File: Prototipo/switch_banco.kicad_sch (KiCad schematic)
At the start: 9 parts

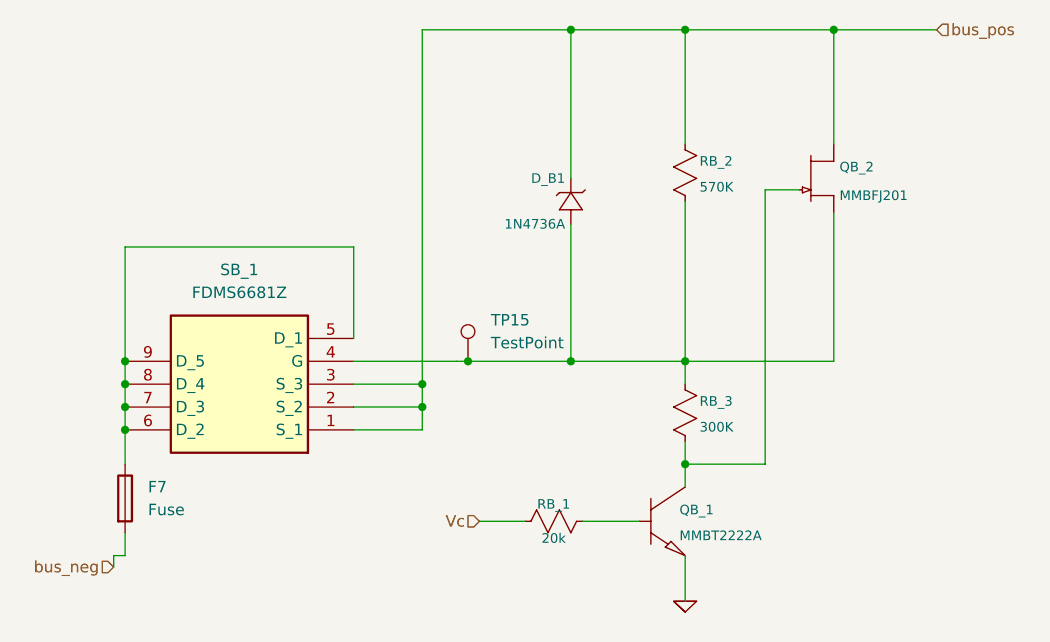
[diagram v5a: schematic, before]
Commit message: termino de reacomodar las celdas con la disposición nueva, faltan las conexiones de la entrada.
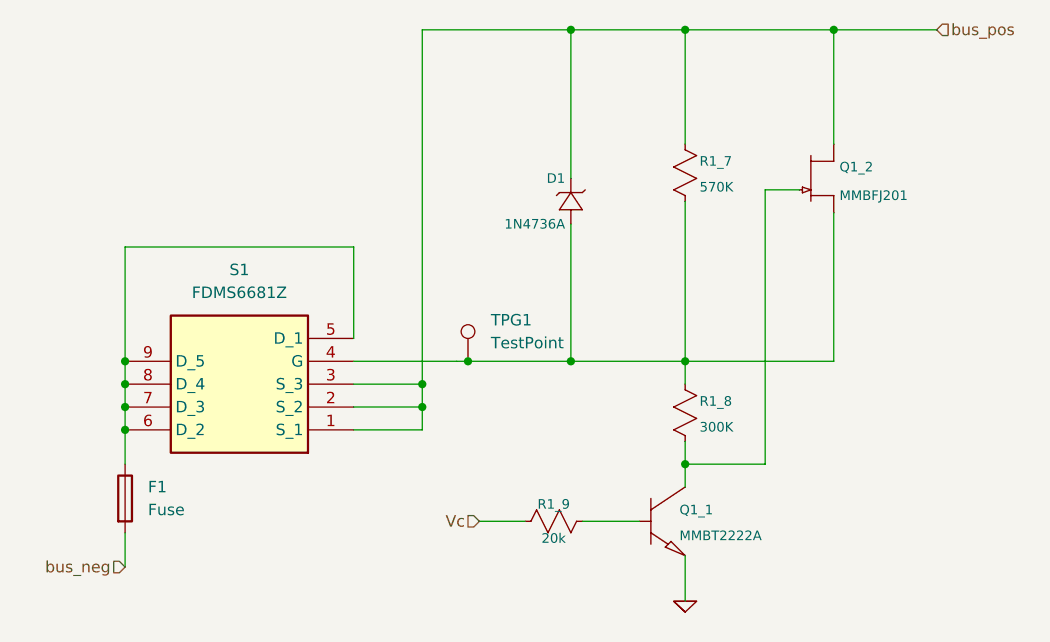
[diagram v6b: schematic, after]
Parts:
- renumbered D_B1 to D1, F7 to F1, QB_1 to Q1_1, QB_2 to Q1_2, RB_2 to R1_7, RB_3 to R1_8, RB_1 to R1_9, SB_1 to S1, TP15 to TPG1
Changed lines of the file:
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@@
 	(wire
 		(pts
-			(xy 62.23 113.03) (xy 62.23 111.76)
+			(xy 63.5 109.22) (xy 63.5 113.03)
 		)
 		(stroke
@@
 	(wire
 		(pts
-			(xy 63.5 111.76) (xy 63.5 109.22)
-		)
-		(stroke
-			(width 0.1524)
-			(type solid)
-		)
-	)
-	(wire
-		(pts
 			(xy 96.52 97.79) (xy 88.9 97.79)
 		)
@@
 		(pts
 			(xy 125.73 92.71) (xy 125.73 90.17)
-		)
-		(stroke
-			(width 0.1524)
-			(type solid)
-		)
-	)
-	(wire
-		(pts
-			(xy 62.23 111.76) (xy 63.5 111.76)
 		)
 		(stroke
@@
 	(hierarchical_label "bus_neg"
 		(shape input)
-		(at 62.23 113.03 180)
+		(at 63.5 113.03 180)
 		(effects
 			(font
@@
 		(on_board yes)
 		(dnp no)
-		(property "Reference" "RB_3"
+		(property "Reference" "R1_8"
 			(at 127.3302 94.615 0)
 			(effects
@@
 			(project "prototipo"
 				(path "/c9225433-a7fd-41e8-8162-e91e829dcb79/69120eb2-13db-48bd-9e77-f62722c18bbc"
-					(reference "RB_9")
+					(reference "R3_8")
 					(unit 1)
 				)
 				(path "/c9225433-a7fd-41e8-8162-e91e829dcb79/7c9a14ee-10ad-4ddf-af17-6bfeb468e011"
-					(reference "RB_3")
+					(reference "R1_8")
 					(unit 1)
 				)
 				(path "/c9225433-a7fd-41e8-8162-e91e829dcb79/aa26f19e-f2c7-49c1-961b-509062eddf74"
-					(reference "RB_6")
+					(reference "R2_8")
 					(unit 1)
 				)
@@
 		(on_board yes)
 		(dnp no)
-		(property "Reference" "QB_1"
+		(property "Reference" "Q1_1"
 			(at 125.095 106.68 0)
 			(effects
@@
 			(project "prototipo"
 				(path "/c9225433-a7fd-41e8-8162-e91e829dcb79/69120eb2-13db-48bd-9e77-f62722c18bbc"
-					(reference "QB_5")
+					(reference "Q3_1")
 					(unit 1)
 				)
 				(path "/c9225433-a7fd-41e8-8162-e91e829dcb79/7c9a14ee-10ad-4ddf-af17-6bfeb468e011"
-					(reference "QB_1")
+					(reference "Q1_1")
 					(unit 1)
 				)
 				(path "/c9225433-a7fd-41e8-8162-e91e829dcb79/aa26f19e-f2c7-49c1-961b-509062eddf74"
-					(reference "QB_3")
+					(reference "Q2_1")
 					(unit 1)
 				)
@@
 		(on_board yes)
 		(dnp no)
-		(property "Reference" "QB_2"
+		(property "Reference" "Q1_2"
 			(at 142.875 68.58 0)
 			(effects
@@
 			(project "prototipo"
 				(path "/c9225433-a7fd-41e8-8162-e91e829dcb79/69120eb2-13db-48bd-9e77-f62722c18bbc"
-					(reference "QB_6")
+					(reference "Q3_2")
 					(unit 1)
 				)
 				(path "/c9225433-a7fd-41e8-8162-e91e829dcb79/7c9a14ee-10ad-4ddf-af17-6bfeb468e011"
-					(reference "QB_2")
+					(reference "Q1_2")
 					(unit 1)
 				)
 				(path "/c9225433-a7fd-41e8-8162-e91e829dcb79/aa26f19e-f2c7-49c1-961b-509062eddf74"
-					(reference "QB_4")
+					(reference "Q2_2")
 					(unit 1)
 				)
@@
 		(on_board yes)
 		(dnp no)
-		(property "Reference" "RB_1"
+		(property "Reference" "R1_9"
 			(at 111.125 106.68 90)
 			(effects
@@
 			(project "prototipo"
 				(path "/c9225433-a7fd-41e8-8162-e91e829dcb79/69120eb2-13db-48bd-9e77-f62722c18bbc"
-					(reference "RB_7")
+					(reference "R3_9")
 					(unit 1)
 				)
 				(path "/c9225433-a7fd-41e8-8162-e91e829dcb79/7c9a14ee-10ad-4ddf-af17-6bfeb468e011"
-					(reference "RB_1")
+					(reference "R1_9")
 					(unit 1)
 				)
 				(path "/c9225433-a7fd-41e8-8162-e91e829dcb79/aa26f19e-f2c7-49c1-961b-509062eddf74"
-					(reference "RB_4")
+					(reference "R2_9")
 					(unit 1)
 				)
@@
 		(on_board yes)
 		(dnp no)
-		(property "Reference" "F7"
+		(property "Reference" "F1"
 			(at 66.04 104.1399 0)
 			(effects
@@
 			(project "prototipo"
 				(path "/c9225433-a7fd-41e8-8162-e91e829dcb79/69120eb2-13db-48bd-9e77-f62722c18bbc"
-					(reference "F9")
+					(reference "F3")
 					(unit 1)
 				)
 				(path "/c9225433-a7fd-41e8-8162-e91e829dcb79/7c9a14ee-10ad-4ddf-af17-6bfeb468e011"
-					(reference "F7")
+					(reference "F1")
 					(unit 1)
 				)
 				(path "/c9225433-a7fd-41e8-8162-e91e829dcb79/aa26f19e-f2c7-49c1-961b-509062eddf74"
-					(reference "F8")
+					(reference "F2")
 					(unit 1)
 				)
@@
 		(on_board yes)
 		(dnp no)
-		(property "Reference" "RB_2"
+		(property "Reference" "R1_7"
 			(at 127.3302 67.945 0)
 			(effects
@@
 			(project "prototipo"
 				(path "/c9225433-a7fd-41e8-8162-e91e829dcb79/69120eb2-13db-48bd-9e77-f62722c18bbc"
-					(reference "RB_8")
+					(reference "R3_7")
 					(unit 1)
 				)
 				(path "/c9225433-a7fd-41e8-8162-e91e829dcb79/7c9a14ee-10ad-4ddf-af17-6bfeb468e011"
-					(reference "RB_2")
+					(reference "R1_7")
 					(unit 1)
 				)
 				(path "/c9225433-a7fd-41e8-8162-e91e829dcb79/aa26f19e-f2c7-49c1-961b-509062eddf74"
-					(reference "RB_5")
+					(reference "R2_7")
 					(unit 1)
 				)
@@
 		(on_board yes)
 		(dnp no)
-		(property "Reference" "D_B1"
+		(property "Reference" "D1"
 			(at 112.395 69.85 0)
 			(effects
@@
 			(project "prototipo"
 				(path "/c9225433-a7fd-41e8-8162-e91e829dcb79/69120eb2-13db-48bd-9e77-f62722c18bbc"
-					(reference "D_B3")
+					(reference "D3")
 					(unit 1)
 				)
 				(path "/c9225433-a7fd-41e8-8162-e91e829dcb79/7c9a14ee-10ad-4ddf-af17-6bfeb468e011"
-					(reference "D_B1")
+					(reference "D1")
 					(unit 1)
 				)
 				(path "/c9225433-a7fd-41e8-8162-e91e829dcb79/aa26f19e-f2c7-49c1-961b-509062eddf74"
-					(reference "D_B2")
+					(reference "D2")
 					(unit 1)
 				)
@@
 		(dnp no)
 		(fields_autoplaced yes)
-		(property "Reference" "TP15"
+		(property "Reference" "TPG1"
 			(at 104.14 85.5979 0)
 			(effects
@@
 			(project "prototipo"
 				(path "/c9225433-a7fd-41e8-8162-e91e829dcb79/69120eb2-13db-48bd-9e77-f62722c18bbc"
-					(reference "TP17")
+					(reference "TPG3")
 					(unit 1)
 				)
 				(path "/c9225433-a7fd-41e8-8162-e91e829dcb79/7c9a14ee-10ad-4ddf-af17-6bfeb468e011"
-					(reference "TP15")
+					(reference "TPG1")
 					(unit 1)
 				)
 				(path "/c9225433-a7fd-41e8-8162-e91e829dcb79/aa26f19e-f2c7-49c1-961b-509062eddf74"
-					(reference "TP16")
+					(reference "TPG2")
 					(unit 1)
 				)
@@
 		(dnp no)
 		(fields_autoplaced yes)
-		(property "Reference" "SB_1"
+		(property "Reference" "S1"
 			(at 76.2 80.01 0)
 			(effects
@@
 			(project ""
 				(path "/c9225433-a7fd-41e8-8162-e91e829dcb79/69120eb2-13db-48bd-9e77-f62722c18bbc"
-					(reference "Q21")
+					(reference "S3")
 					(unit 1)
 				)
 				(path "/c9225433-a7fd-41e8-8162-e91e829dcb79/7c9a14ee-10ad-4ddf-af17-6bfeb468e011"
-					(reference "SB_1")
+					(reference "S1")
 					(unit 1)
 				)
 				(path "/c9225433-a7fd-41e8-8162-e91e829dcb79/aa26f19e-f2c7-49c1-961b-509062eddf74"
-					(reference "Q20")
-					(unit 1)
-				)
+					(reference "S2")
+					(unit 1)
+				)

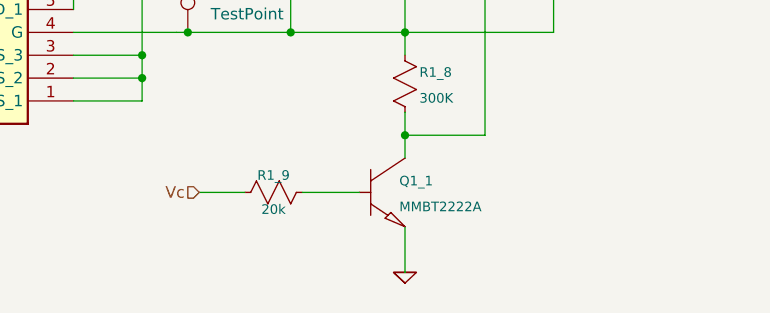
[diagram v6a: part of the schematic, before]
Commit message: Propuesta de conexión de las entradas
no me gusta la opción, pero esta conectado
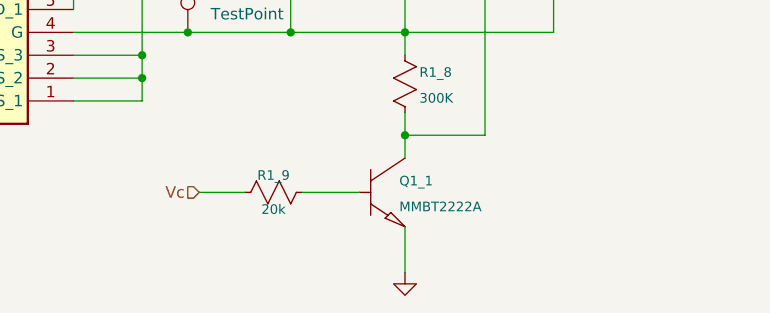
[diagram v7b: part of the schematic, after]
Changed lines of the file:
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@@
 	)
 	(symbol
-		(lib_id "ltspice:GND")
+		(lib_id "power:GND")
 		(at 125.73 116.84 0)
 		(unit 1)
@@
 			)
 		)
-		(property "Description" ""
+		(property "Description" "Power symbol creates a global label with name \"GND\" , ground"
 			(at 125.73 116.84 0)
 			(effects
@@
 			)
 		)
-		(pin ""
+		(pin "1"
 		)
 		(instances

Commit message: Sumo ultimos cambios hablados en reunion
agrega agujeros para tornillos, jumper para banco 1, INVERSOR CON ZOCALO, cambia el diametro de test points y vias, acomoda serigrafia, SIN WARNINGS
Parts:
- S1: footprint FDMS6681Z -> Huellas:FDMS6681Z
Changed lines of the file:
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@@
 			)
 		)
-		(property "Footprint" "FDMS6681Z"
+		(property "Footprint" "Huellas:FDMS6681Z"
 			(at 67.31 2.87 0)
 			(effects
